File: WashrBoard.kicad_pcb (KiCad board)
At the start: 2 copper layers, 70 x 50 mm, 37 parts, among them J1 TestPoint 5V, J10 ProgPoint GND, J2 USB_C_Receptacle_USB2.0_16P, J3 TestPoint GND, J4 TestPoint 3.3V, J5 JST GH, J6 ProgPoint 5V, J7 ProgPoint P9 GND, J8 ProgPointPoint D_P, J9 ProgPoint D_N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

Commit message: Updated version, and moved old designs to archive repo
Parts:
- added G***: LOGO, Footprints:SpaceOnaLogo, F.Cu at (178.5, 44.5)
- moved J2 0.50 mm to (123.5, 65.1)
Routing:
- net VBUS: track 106.8 -> 117.1 mm, vias 5 -> 6
- net +3.3V: track 180.1 -> 179.0 mm, vias 6 -> 8
- net GND: track 241.9 -> 240.9 mm
- net /D_P: track 62.4 -> 61.4 mm
- net Net-(J2-CC2): track 27.1 -> 26.6 mm
- net Net-(J2-CC1): track 25.6 -> 25.1 mm
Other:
- board text added: "Only use one connector at a time"
- board text added: "SpaceOna Washr V 5.0"
- board text added: "© Robbie Leslie 2025"

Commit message: Updated silkscreen
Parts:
- J5: value JST GH -> JST XH
- MT1: value ~ -> IMU
- U1: value ~ -> Regulator

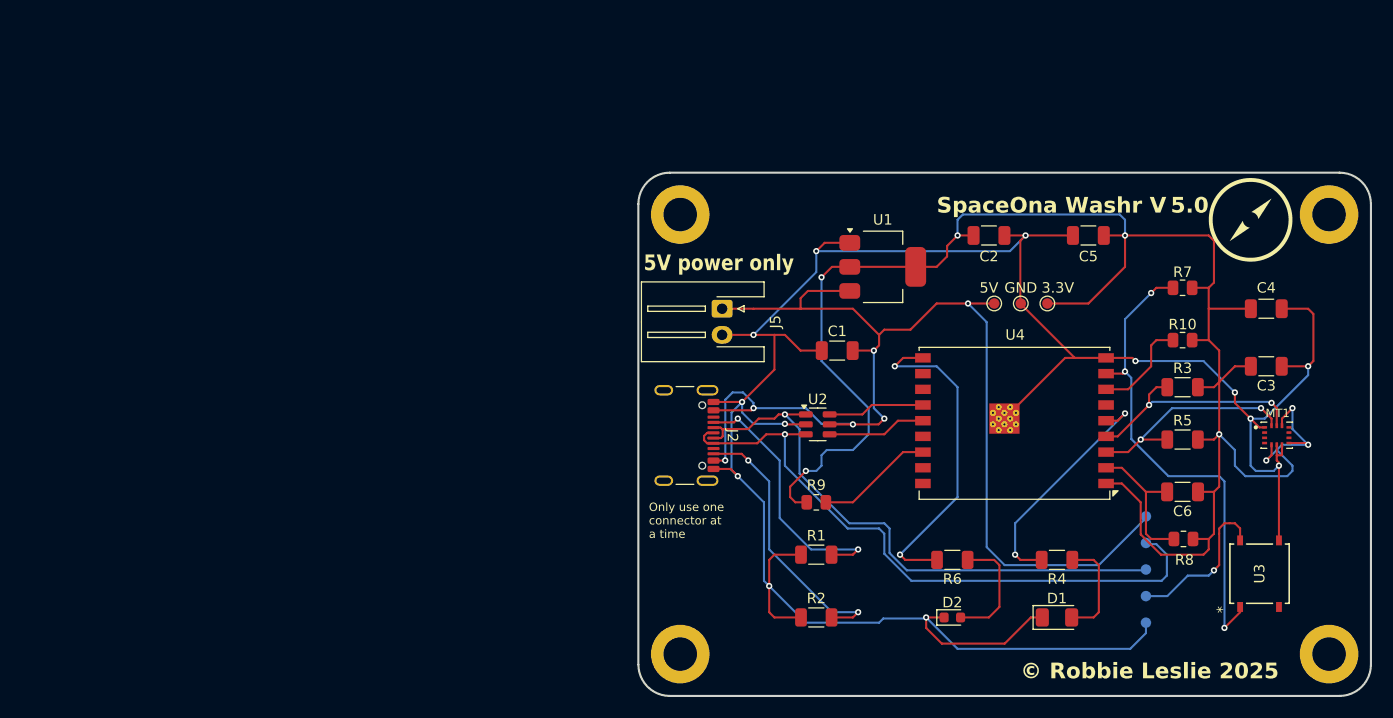
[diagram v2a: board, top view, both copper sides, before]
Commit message: Added details to PCB drawing
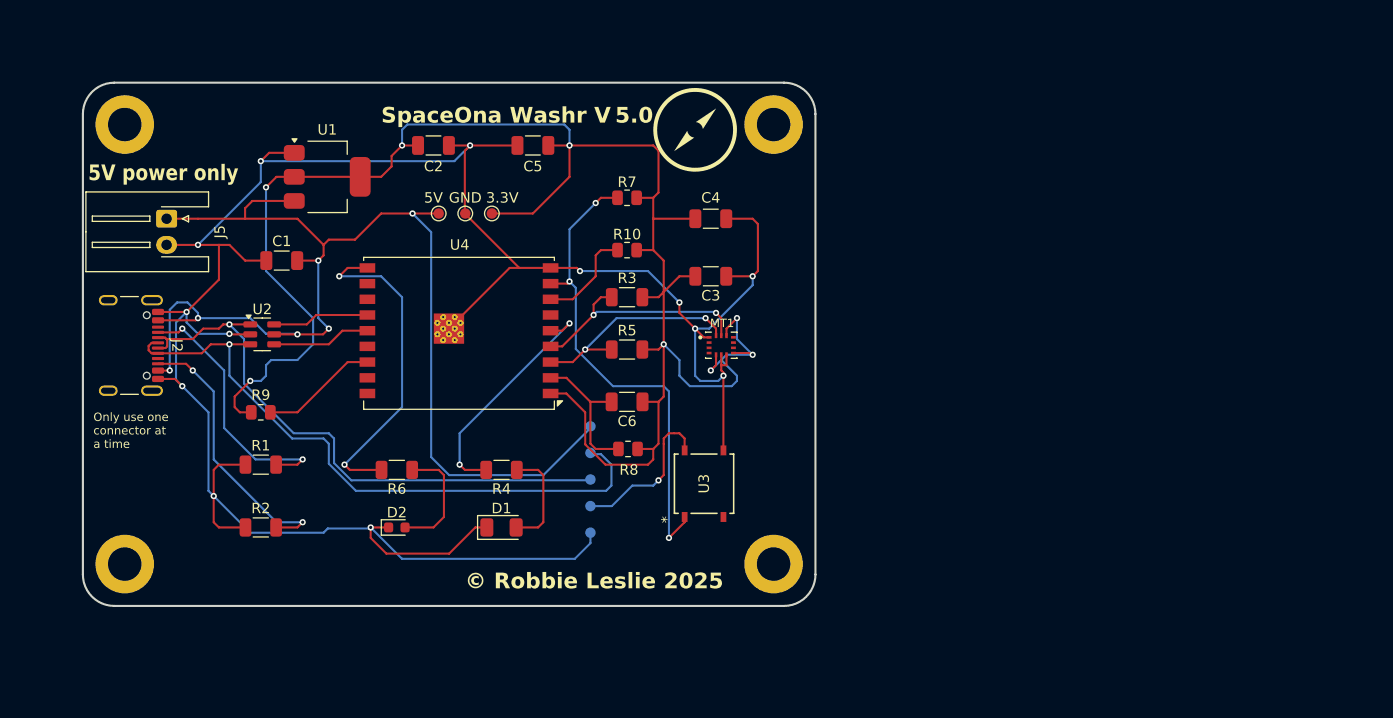
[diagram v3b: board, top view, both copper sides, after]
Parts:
- moved H2 53.8 mm to (132.9, 35.4)
- moved H4 53.8 mm to (132.9, 77.4)
- moved J4 53.8 mm to (106.0, 43.9)
- moved J6 53.8 mm to (115.4, 64.2)
- moved J9 53.8 mm to (115.4, 69.3)
- moved MT1 53.8 mm to (127.9, 56.5)
- moved R8 53.8 mm to (119.0, 66.4)
- moved U3 53.8 mm to (126.3, 69.7)
- moved C1 53.8 mm to (85.9, 48.4)
- moved C2 53.8 mm to (100.4, 37.4)
- moved C3 53.8 mm to (126.9, 49.9)
- moved C4 53.8 mm to (126.9, 44.4)
- moved C5 53.8 mm to (109.9, 37.4)
- moved C6 53.8 mm to (118.9, 61.9)
- moved D1 53.8 mm to (106.9, 73.9)
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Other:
- board text added: "1/19/2025"
- board text added: "By Robbie Leslie"
- board text added: "V5.0"
- board text added: "Washr Board"

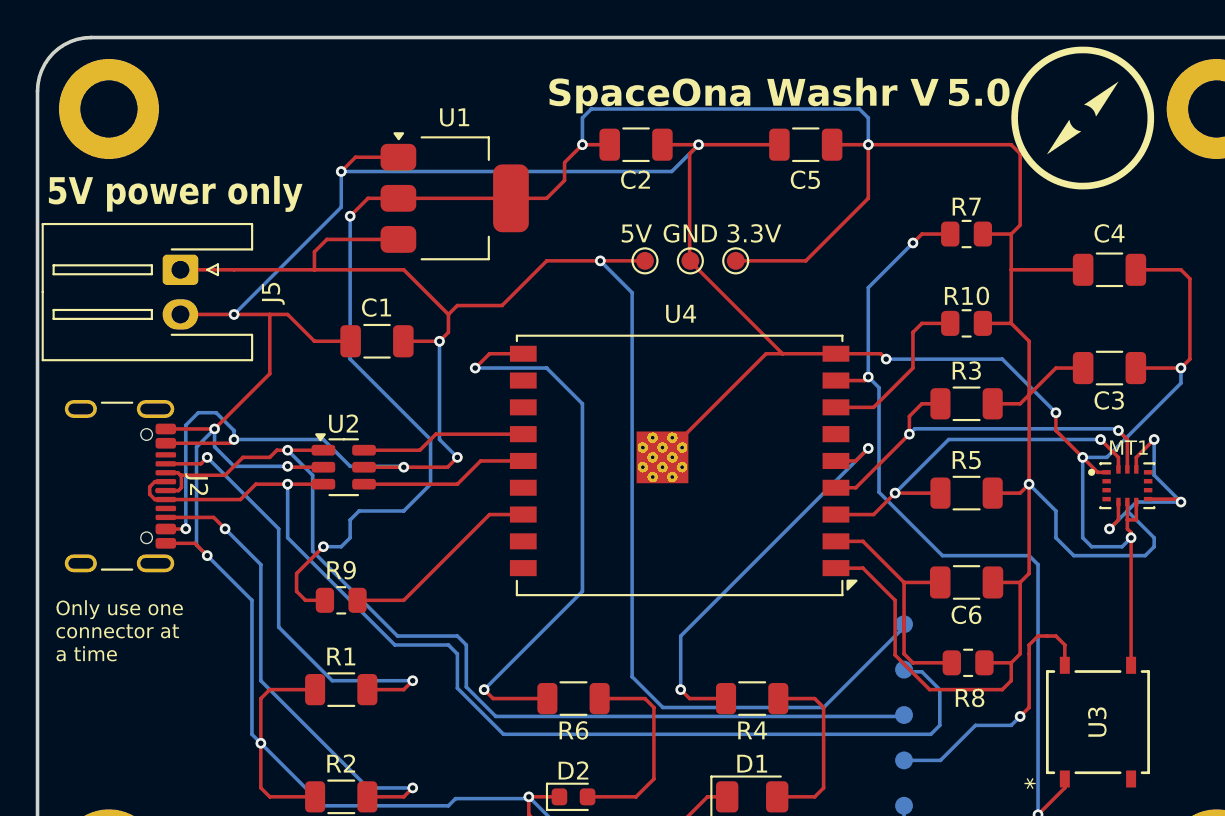
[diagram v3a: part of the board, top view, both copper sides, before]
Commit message: Swapped JST XH for GH connector
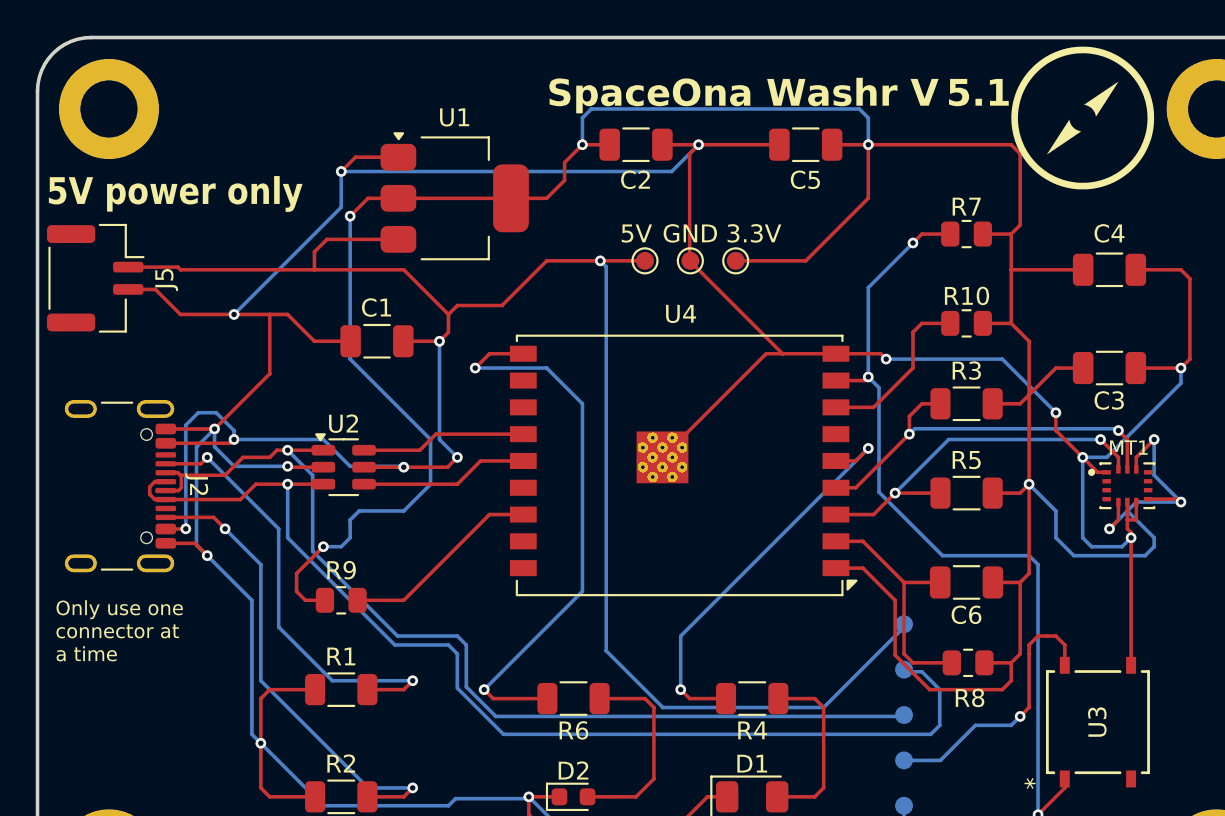
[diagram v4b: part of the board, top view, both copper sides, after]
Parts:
- J5: value JST XH -> JST GH; footprint Connector_JST:JST_XH_S2B-XH-A-1_1x02_P2.50mm_Horizontal -> Connector_JST:JST_GH_SM02B-GHS-TB_1x02-1MP_P1.25mm_Horizontal
- moved J5 4.79 mm to (70.2, 44.9)
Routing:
- net GND: track 240.9 -> 245.2 mm
- net VBUS: track 117.1 -> 120.8 mm
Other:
- board text added: "1/26/2025"
- board text added: "SpaceOna Washr V 5.1"
- board text added: "V5.1"
- board text removed: "1/19/2025"
- board text removed: "SpaceOna Washr V 5.0"
- board text removed: "V5.0"

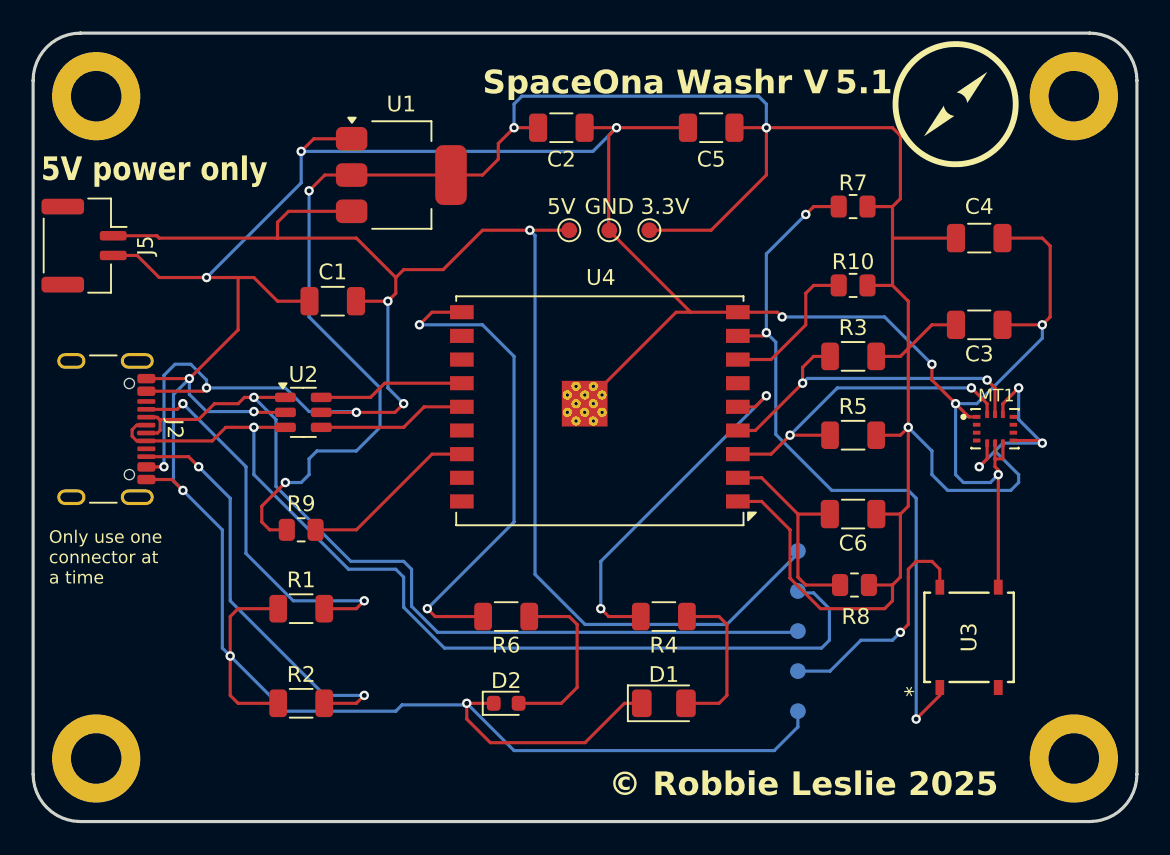
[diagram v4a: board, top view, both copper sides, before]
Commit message: Swapped screwholes to ISO 7380
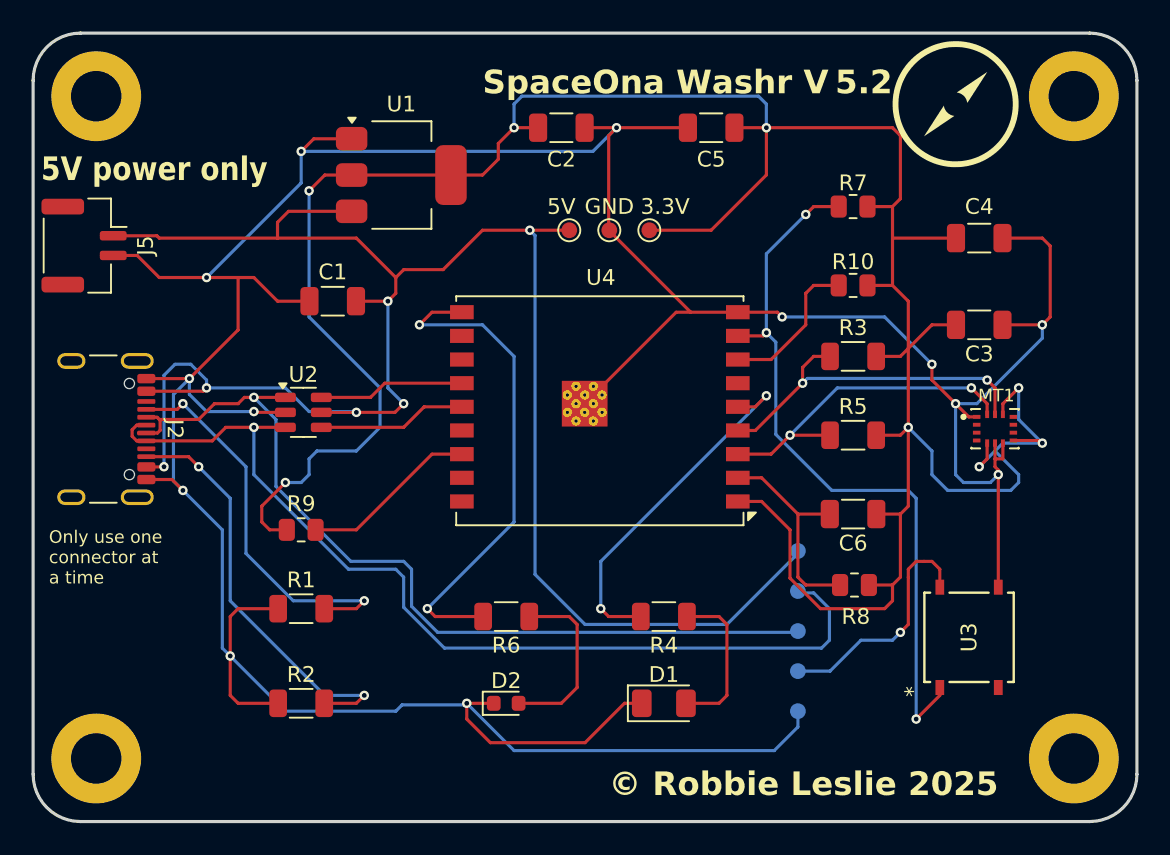
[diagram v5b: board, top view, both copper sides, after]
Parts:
- H1, H2, H3, H4: footprint MountingHole:MountingHole_3.2mm_M3_DIN965_Pad -> MountingHole:MountingHole_3.2mm_M3_ISO7380_Pad
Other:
- board text added: "2/1/2025"
- board text added: "SpaceOna Washr V 5.2"
- board text added: "V5.2"
- board text removed: "1/26/2025"
- board text removed: "SpaceOna Washr V 5.1"
- board text removed: "V5.1"
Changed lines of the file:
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@@
 			(usegerberattributes yes)
 			(usegerberadvancedattributes yes)
-			(creategerberjobfile yes)
+			(creategerberjobfile no)
 			(dashed_line_dash_ratio 12.000000)
 			(dashed_line_gap_ratio 3.000000)
@@
 			(plotinvisibletext no)
 			(sketchpadsonfab no)
-			(subtractmaskfromsilk no)
+			(subtractmaskfromsilk yes)
 			(outputformat 1)
 			(mirror no)
-			(drillshape 1)
+			(drillshape 0)
 			(scaleselection 1)
-			(outputdirectory "")
+			(outputdirectory "Outputs/V5.2/Gerbers/")
 		)
 	)
@@
 	(net 31 "unconnected-(U4-IO0-Pad18)")
 	(net 32 "unconnected-(U4-IO20{slash}RXD-Pad11)")
-	(footprint "MountingHole:MountingHole_3.2mm_M3_DIN965_Pad"
+	(footprint "MountingHole:MountingHole_3.2mm_M3_ISO7380_Pad"
 		(layer "F.Cu")
 		(at 132.92 35.4)
-		(descr "Mounting Hole 3.2mm, M3, DIN965")
-		(tags "mounting hole 3.2mm m3 din965")
+		(descr "Mounting Hole 3.2mm, M3, ISO7380")
+		(tags "mounting hole 3.2mm m3 iso7380")
 		(property "Reference" "H2"
-			(at 0 -3.8 0)
+			(at 0 -3.85 0)
 			(layer "F.SilkS")
 			(hide yes)
@@
 		)
 		(property "Value" "MountingHole"
-			(at 0 3.8 0)
+			(at 0 3.85 0)
 			(layer "F.Fab")
-			(hide yes)
 			(effects
 				(font
@@
 			)
 		)
-		(property "Footprint" "MountingHole:MountingHole_3.2mm_M3_DIN965_Pad"
+		(property "Footprint" "MountingHole:MountingHole_3.2mm_M3_ISO7380_Pad"
 			(at 0 0 0)
 			(unlocked yes)
@@
 		(fp_circle
 			(center 0 0)
-			(end 2.8 0)
+			(end 2.85 0)
 			(stroke
 				(width 0.15)
@@
 		(fp_circle
 			(center 0 0)
-			(end 3.05 0)
+			(end 3.1 0)
 			(stroke
 				(width 0.05)
@@
 		(pad "1" thru_hole circle
 			(at 0 0)
-			(size 5.6 5.6)
+			(size 5.7 5.7)
 			(drill 3.2)
 			(layers "*.Cu" "*.Mask")
@@
 		)
 	)
-	(footprint "MountingHole:MountingHole_3.2mm_M3_DIN965_Pad"
+	(footprint "MountingHole:MountingHole_3.2mm_M3_ISO7380_Pad"
 		(layer "F.Cu")
 		(at 70.92 35.4)
-		(descr "Mounting Hole 3.2mm, M3, DIN965")
-		(tags "mounting hole 3.2mm m3 din965")
+		(descr "Mounting Hole 3.2mm, M3, ISO7380")
+		(tags "mounting hole 3.2mm m3 iso7380")
 		(property "Reference" "H1"
-			(at 0 -3.8 0)
+			(at 0 -3.85 0)
 			(layer "F.SilkS")
 			(hide yes)
@@
 		)
 		(property "Value" "MountingHole"
-			(at 0 3.8 0)
+			(at 0 3.85 0)
 			(layer "F.Fab")
-			(hide yes)
 			(effects
 				(font
@@
 			)
 		)
-		(property "Footprint" "MountingHole:MountingHole_3.2mm_M3_DIN965_Pad"
+		(property "Footprint" "MountingHole:MountingHole_3.2mm_M3_ISO7380_Pad"
 			(at 0 0 0)
 			(unlocked yes)
@@
 		(fp_circle
 			(center 0 0)
-			(end 2.8 0)
+			(end 2.85 0)
 			(stroke
 				(width 0.15)
@@
 		(fp_circle
 			(center 0 0)
-			(end 3.05 0)
+			(end 3.1 0)
 			(stroke
 				(width 0.05)
@@
 		(pad "1" thru_hole circle
 			(at 0 0)
-			(size 5.6 5.6)
+			(size 5.7 5.7)
 			(drill 3.2)
 			(layers "*.Cu" "*.Mask")
@@
 		)
 	)
-	(footprint "MountingHole:MountingHole_3.2mm_M3_DIN965_Pad"
+	(footprint "MountingHole:MountingHole_3.2mm_M3_ISO7380_Pad"
 		(layer "F.Cu")
 		(at 70.92 77.4)
-		(descr "Mounting Hole 3.2mm, M3, DIN965")
-		(tags "mounting hole 3.2mm m3 din965")
+		(descr "Mounting Hole 3.2mm, M3, ISO7380")
+		(tags "mounting hole 3.2mm m3 iso7380")
 		(property "Reference" "H3"
-			(at 0 -3.8 0)
+			(at 0 -3.85 0)
 			(layer "F.SilkS")
 			(hide yes)
@@
 		)
 		(property "Value" "MountingHole"
-			(at 0 3.8 0)
+			(at 0 3.85 0)
 			(layer "F.Fab")
-			(hide yes)
 			(effects
 				(font
@@
 			)
 		)
-		(property "Footprint" "MountingHole:MountingHole_3.2mm_M3_DIN965_Pad"
+		(property "Footprint" "MountingHole:MountingHole_3.2mm_M3_ISO7380_Pad"
 			(at 0 0 0)
 			(unlocked yes)
@@
 		(fp_circle
 			(center 0 0)
-			(end 2.8 0)
+			(end 2.85 0)
 			(stroke
 				(width 0.15)
@@
 		(fp_circle
 			(center 0 0)
-			(end 3.05 0)
+			(end 3.1 0)
 			(stroke
 				(width 0.05)
@@
 		(pad "1" thru_hole circle
 			(at 0 0)
-			(size 5.6 5.6)
+			(size 5.7 5.7)
 			(drill 3.2)
 			(layers "*.Cu" "*.Mask")
@@
 		)
 	)
-	(footprint "MountingHole:MountingHole_3.2mm_M3_DIN965_Pad"
+	(footprint "MountingHole:MountingHole_3.2mm_M3_ISO7380_Pad"
 		(layer "F.Cu")
 		(at 132.92 77.4)
-		(descr "Mounting Hole 3.2mm, M3, DIN965")
-		(tags "mounting hole 3.2mm m3 din965")
+		(descr "Mounting Hole 3.2mm, M3, ISO7380")
+		(tags "mounting hole 3.2mm m3 iso7380")
 		(property "Reference" "H4"
-			(at 0 -3.8 0)
+			(at 0 -3.85 0)
 			(layer "F.SilkS")
 			(hide yes)
@@
 		)
 		(property "Value" "MountingHole"
-			(at 0 3.8 0)
+			(at 0 3.85 0)
 			(layer "F.Fab")
-			(hide yes)
 			(effects
 				(font
@@
 			)
 		)
-		(property "Footprint" "MountingHole:MountingHole_3.2mm_M3_DIN965_Pad"
+		(property "Footprint" "MountingHole:MountingHole_3.2mm_M3_ISO7380_Pad"
 			(at 0 0 0)
 			(unlocked yes)
@@
 		(fp_circle
 			(center 0 0)
-			(end 2.8 0)
+			(end 2.85 0)
 			(stroke
 				(width 0.15)
@@
 		(fp_circle
 			(center 0 0)
-			(end 3.05 0)
+			(end 3.1 0)
 			(stroke
 				(width 0.05)
@@
 		(pad "1" thru_hole circle
 			(at 0 0)
-			(size 5.6 5.6)
+			(size 5.7 5.7)
 			(drill 3.2)
 			(layers "*.Cu" "*.Mask")
@@
 		)
 	)
-	(gr_text "SpaceOna Washr V 5.1"
+	(gr_text "SpaceOna Washr V 5.2"
 		(at 95.42 35.4 0)
 		(layer "F.SilkS")
@@
 		)
 	)
-	(gr_text "1/26/2025"
+	(gr_text "2/1/2025"
 		(at 119 132 0)
 		(layer "Cmts.User")
@@
 		)
 	)
-	(gr_text "V5.1"
+	(gr_text "V5.2"
 		(at 181 132 0)
 		(layer "Cmts.User")
